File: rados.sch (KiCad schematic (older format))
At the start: 1 part

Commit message: More schematics, some layout
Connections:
- net CS0: now reaches SHIELD1.10 (D10)
- net SD_CD: now reaches SHIELD1.14 (D14-TX3)
- net Z-EN: now reaches SHIELD1.15 (D15-RX3)
- net Y-DIR: now reaches SHIELD1.16 (D16-TX2)
- net Y-STEP: now reaches SHIELD1.17 (D17-RX2)
- net Z-STEP: now reaches SHIELD1.2 (D2)
- net SDA: now reaches SHIELD1.20 (D20-SDA)
- net SCL: now reaches SHIELD1.21 (D21-SCL)
- net Y-EN: now reaches SHIELD1.22 (D22)
- net X-DIR: now reaches SHIELD1.23 (D23)
- net X-STEP: now reaches SHIELD1.24 (D24)
- net X-EN: now reaches SHIELD1.26 (D26)
- net X-: now reaches SHIELD1.28 (D28)
- net Z-DIR: now reaches SHIELD1.3 (D3)
- net Y-: now reaches SHIELD1.30 (D30)
- net Z-: now reaches SHIELD1.32 (D32)
- net X+: now reaches SHIELD1.34 (D34)
- net Y+: now reaches SHIELD1.36 (D36)
- net Z+: now reaches SHIELD1.38 (D38)
- net CS1: now reaches SHIELD1.4 (D4)
- net LCD_RS: now reaches SHIELD1.42 (D42)
- net LCD_E: now reaches SHIELD1.43 (D43)
- net LCD_4: now reaches SHIELD1.44 (D44)
- net LCD_5: now reaches SHIELD1.45 (D45)
- net LCD_6: now reaches SHIELD1.46 (D46)
- net LCD_7: now reaches SHIELD1.47 (D47)
- net ENC_SW: now reaches SHIELD1.48 (D48)
- net E3-EN: now reaches SHIELD1.49 (D49)
- net ENC_B: now reaches SHIELD1.50 (D50-MISO)
- net E3-STEP: now reaches SHIELD1.51 (D51-MOSI)
- net ENC_A: now reaches SHIELD1.52 (D52-SCK)
- net E3-DIR: now reaches SHIELD1.53 (D53-SS)
- net T0: now reaches SHIELD1.AD0
- net T1: now reaches SHIELD1.AD1
- net E2-STEP: now reaches SHIELD1.AD10
- net E2-EN: now reaches SHIELD1.AD11
- net T2: now reaches SHIELD1.AD2
- net T3: now reaches SHIELD1.AD3
- net T4: now reaches SHIELD1.AD4
- net E1-DIR: now reaches SHIELD1.AD6
- net E1-STEP: now reaches SHIELD1.AD7
- net E1-EN: now reaches SHIELD1.AD8
- net E2-DIR: now reaches SHIELD1.AD9
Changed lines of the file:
@@
 	1    0    0    -1
 $EndComp
-Text GLabel 3100 2200 0    47   Input ~ 0
+Text GLabel 3000 2200 0    47   Input ~ 0
 RESET
 $Comp
@@
 L +3.3V #PWR02
 U 1 1 568A9448
-P 2700 2275
-F 0 "#PWR02" H 2700 2125 50  0001 C CNN
-F 1 "+3.3V" H 2718 2449 50  0000 C CNN
-F 2 "" H 2700 2275 50  0000 C CNN
-F 3 "" H 2700 2275 50  0000 C CNN
-	1    2700 2275
-	1    0    0    -1
-$EndComp
-Wire Wire Line
-	2700 2300 3100 2300
-Wire Wire Line
-	2700 2300 2700 2275
+P 2650 2275
+F 0 "#PWR02" H 2650 2125 50  0001 C CNN
+F 1 "+3.3V" H 2625 2400 50  0000 C CNN
+F 2 "" H 2650 2275 50  0000 C CNN
+F 3 "" H 2650 2275 50  0000 C CNN
+	1    2650 2275
+	1    0    0    -1
+$EndComp
+Wire Wire Line
+	2650 2300 3100 2300
 $Comp
 L +5V #PWR03
@@
 P 2525 2400
 F 0 "#PWR03" H 2525 2250 50  0001 C CNN
-F 1 "+5V" H 2543 2574 50  0000 C CNN
+F 1 "+5V" H 2500 2525 50  0000 C CNN
 F 2 "" H 2525 2400 50  0000 C CNN
 F 3 "" H 2525 2400 50  0000 C CNN
@@
 F1 "power.sch" 59
 $EndSheet
-Text GLabel 3100 2700 0    47   Input ~ 0
+Text GLabel 3000 2700 0    47   Input ~ 0
 ARDUINO-VIN
 $Sheet
@@
 F1 "misc.sch" 60
 $EndSheet
+Text GLabel 5100 2300 2    47   Output ~ 0
+CS0
+Text GLabel 5100 3000 2    47   Output ~ 0
+CS1
+Wire Wire Line
+	5100 3000 5000 3000
+Wire Wire Line
+	5100 2300 5000 2300
+Text GLabel 5100 3100 2    47   Output ~ 0
+Z-DIR
+Text GLabel 5100 3200 2    47   Output ~ 0
+Z-STEP
+Wire Wire Line
+	5000 3100 5100 3100
+Wire Wire Line
+	5000 3200 5100 3200
+Text GLabel 5125 3600 2    47   Input ~ 0
+SD_CD
+Text GLabel 5125 3700 2    47   Output ~ 0
+Z-EN
+Text GLabel 5125 3800 2    47   Output ~ 0
+Y-DIR
+Text GLabel 5125 3900 2    47   Output ~ 0
+Y-STEP
+Text GLabel 5125 4200 2    47   BiDi ~ 0
+SDA
+Text GLabel 5125 4300 2    47   BiDi ~ 0
+SCL
+$Comp
+L +5V #PWR?
+U 1 1 568ECF51
+P 5000 4650
+F 0 "#PWR?" H 5000 4500 50  0001 C CNN
+F 1 "+5V" H 5018 4824 50  0000 C CNN
+F 2 "" H 5000 4650 50  0000 C CNN
+F 3 "" H 5000 4650 50  0000 C CNN
+	1    5000 4650
+	1    0    0    -1
+$EndComp
+Wire Wire Line
+	5125 3600 5000 3600
+Wire Wire Line
+	5125 3700 5000 3700
+Wire Wire Line
+	5125 3800 5000 3800
+Wire Wire Line
+	5125 3900 5000 3900
+Wire Wire Line
+	5000 4200 5125 4200
+Wire Wire Line
+	5125 4300 5000 4300
+Wire Wire Line
+	5000 4650 5000 4850
+Connection ~ 5000 4750
+Text GLabel 5125 5050 2    47   Output ~ 0
+Y-EN
+Text GLabel 5125 5150 2    47   Output ~ 0
+X-DIR
+Text GLabel 5125 5250 2    47   Output ~ 0
+X-STEP
+Text GLabel 5125 5450 2    47   Output ~ 0
+X-EN
+Text GLabel 5125 5650 2    47   Input ~ 0
+X-
+Text GLabel 5125 5900 2    47   Input ~ 0
+Y-
+Text GLabel 5125 6100 2    47   Input ~ 0
+Z-
+Text GLabel 5125 6300 2    47   Input ~ 0
+X+
+Text GLabel 5125 6500 2    47   Input ~ 0
+Y+
+Text GLabel 3000 6600 0    47   Input ~ 0
+Z+
+Wire Wire Line
+	5000 5050 5125 5050
+Wire Wire Line
+	5125 5150 5000 5150
+Wire Wire Line
+	5000 5250 5125 5250
+Wire Wire Line
+	5000 5450 5125 5450
+Wire Wire Line
+	5125 5650 5000 5650
+Wire Wire Line
+	5000 5900 5125 5900
+Wire Wire Line
+	5125 6100 5000 6100
+Wire Wire Line
+	5000 6300 5125 6300
+Wire Wire Line
+	5125 6500 5000 6500
+Wire Wire Line
+	3000 6600 3100 6600
+Text GLabel 3000 6150 0    47   BiDi ~ 0
+LCD_RS
+Text GLabel 3000 6050 0    47   BiDi ~ 0
+LCD_E
+Text GLabel 3000 5950 0    47   BiDi ~ 0
+LCD_4
+Text GLabel 3000 5850 0    47   BiDi ~ 0
+LCD_5
+Text GLabel 3000 5750 0    47   BiDi ~ 0
+LCD_6
+Text GLabel 3000 5650 0    47   BiDi ~ 0
+LCD_7
+Text GLabel 3000 5550 0    47   BiDi ~ 0
+ENC_SW
+Text GLabel 3000 5300 0    47   BiDi ~ 0
+ENC_B
+Text GLabel 3000 5100 0    47   BiDi ~ 0
+ENC_A
+Wire Wire Line
+	3000 6150 3100 6150
+Wire Wire Line
+	3100 6050 3000 6050
+Wire Wire Line
+	3000 5950 3100 5950
+Wire Wire Line
+	3100 5850 3000 5850
+Wire Wire Line
+	3000 5750 3100 5750
+Wire Wire Line
+	3100 5650 3000 5650
+Wire Wire Line
+	3000 5550 3100 5550
+Wire Wire Line
+	3000 5300 3100 5300
+Wire Wire Line
+	3100 5100 3000 5100
+Text GLabel 3000 5450 0    47   Output ~ 0
+E3-EN
+Text GLabel 3000 5200 0    47   Output ~ 0
+E3-STEP
+Text GLabel 3000 5000 0    47   Output ~ 0
+E3-DIR
+Wire Wire Line
+	3000 5000 3100 5000
+Wire Wire Line
+	3100 5200 3000 5200
+Wire Wire Line
+	3000 5450 3100 5450
+$Comp
+L GND #PWR?
+U 1 1 568EE3CA
+P 3100 4850
+F 0 "#PWR?" H 3100 4600 50  0001 C CNN
+F 1 "GND" H 3108 4676 50  0000 C CNN
+F 2 "" H 3100 4850 50  0000 C CNN
+F 3 "" H 3100 4850 50  0000 C CNN
+	1    3100 4850
+	1    0    0    -1
+$EndComp
+Wire Wire Line
+	3100 4850 3100 4750
+Connection ~ 3100 4850
+Text GLabel 3000 4000 0    47   Output ~ 0
+E2-STEP
+Text GLabel 3000 4100 0    47   Output ~ 0
+E2-EN
+Text GLabel 3000 3900 0    47   Output ~ 0
+E2-DIR
+Wire Wire Line
+	3000 4100 3100 4100
+Wire Wire Line
+	3100 4000 3000 4000
+Wire Wire Line
+	3000 3900 3100 3900
+Text GLabel 3000 3600 0    47   Output ~ 0
+E1-STEP
+Text GLabel 3000 3800 0    47   Output ~ 0
+E1-EN
+Text GLabel 3000 3500 0    47   Output ~ 0
+E1-DIR
+Wire Wire Line
+	3000 3800 3100 3800
+Wire Wire Line
+	3100 3600 3000 3600
+Wire Wire Line
+	3000 3500 3100 3500
+Wire Wire Line
+	3000 2700 3100 2700
+Wire Wire Line
+	2650 2300 2650 2275
+Wire Wire Line
+	3000 2200 3100 2200
+Text GLabel 3000 2900 0    47   Input ~ 0
+T0
+Text GLabel 3000 3000 0    47   Input ~ 0
+T1
+Text GLabel 3000 3100 0    47   Input ~ 0
+T2
+Text GLabel 3000 3200 0    47   Input ~ 0
+T3
+Text GLabel 3000 3300 0    47   Input ~ 0
+T4
+Wire Wire Line
+	3000 2900 3100 2900
+Wire Wire Line
+	3100 3000 3000 3000
+Wire Wire Line
+	3000 3100 3100 3100
+Wire Wire Line
+	3100 3200 3000 3200
+Wire Wire Line
+	3000 3300 3100 3300
 $EndSCHEMATC

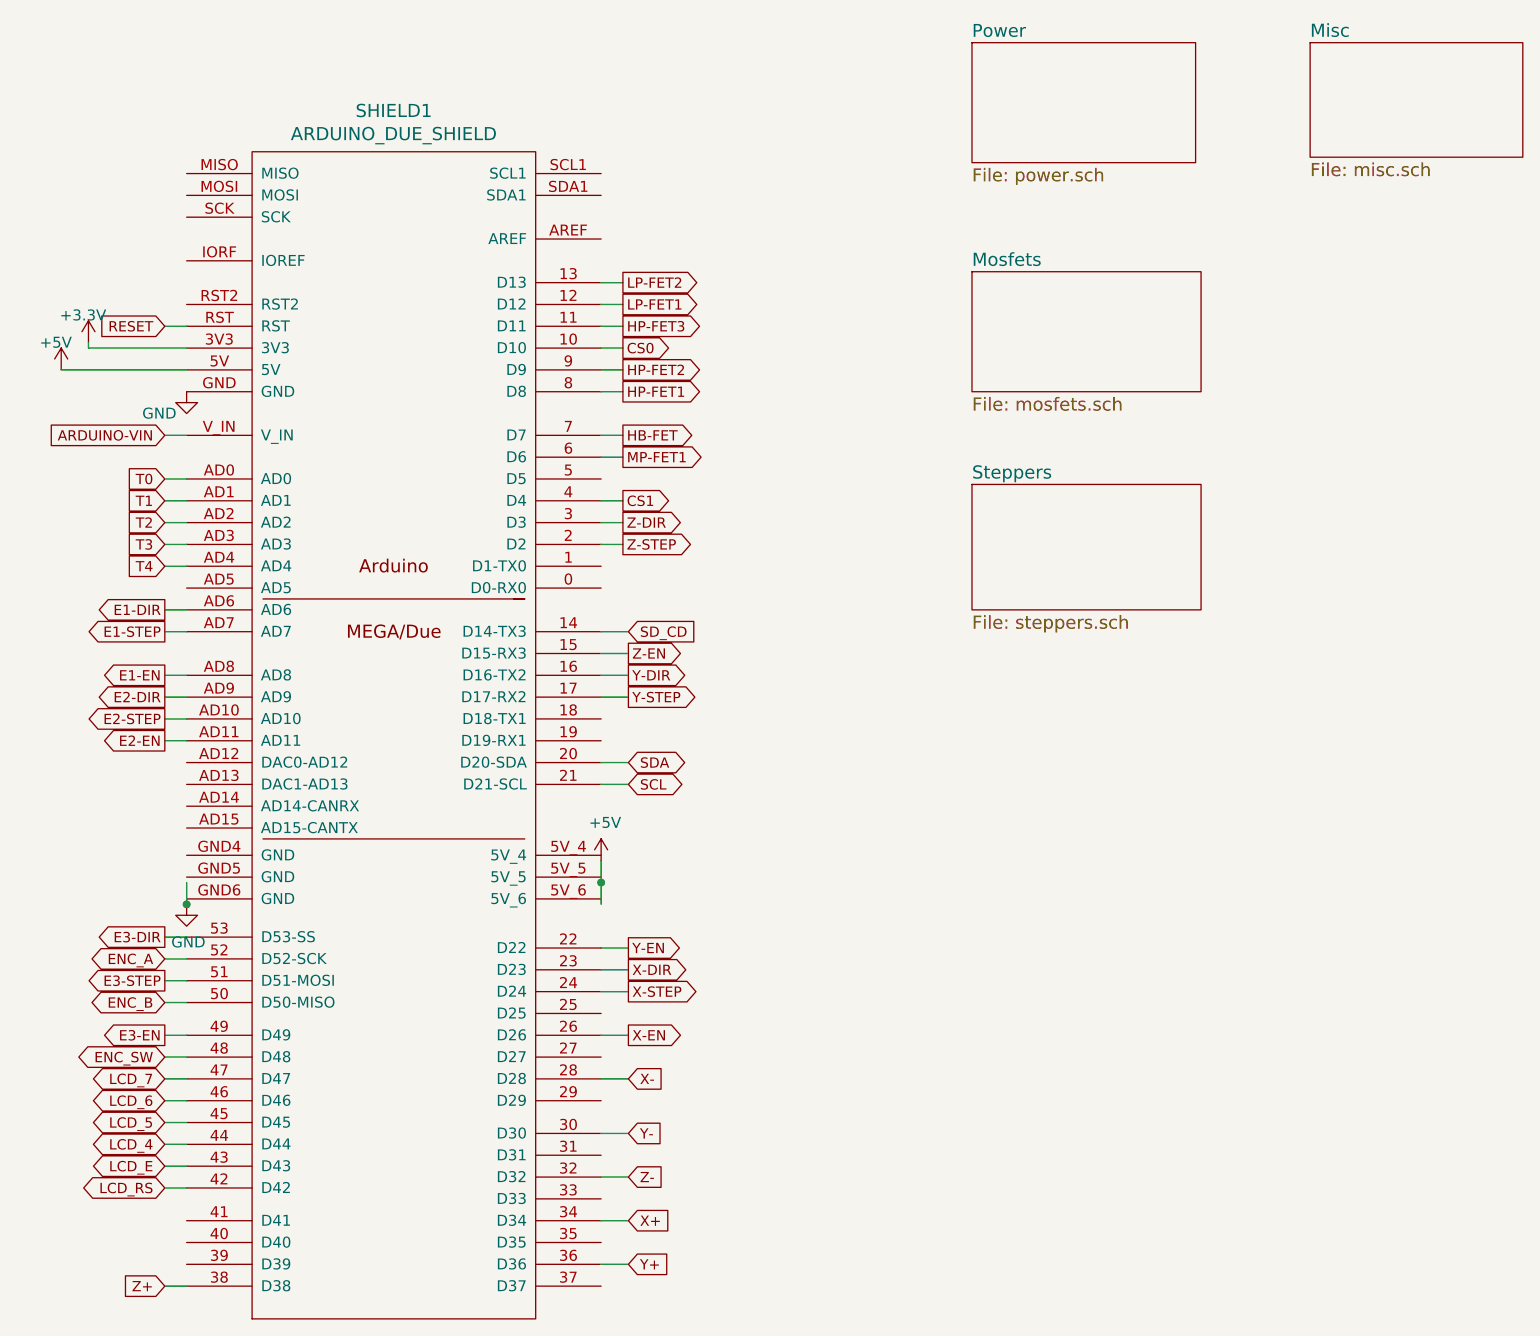
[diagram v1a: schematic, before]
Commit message: more placement and routing
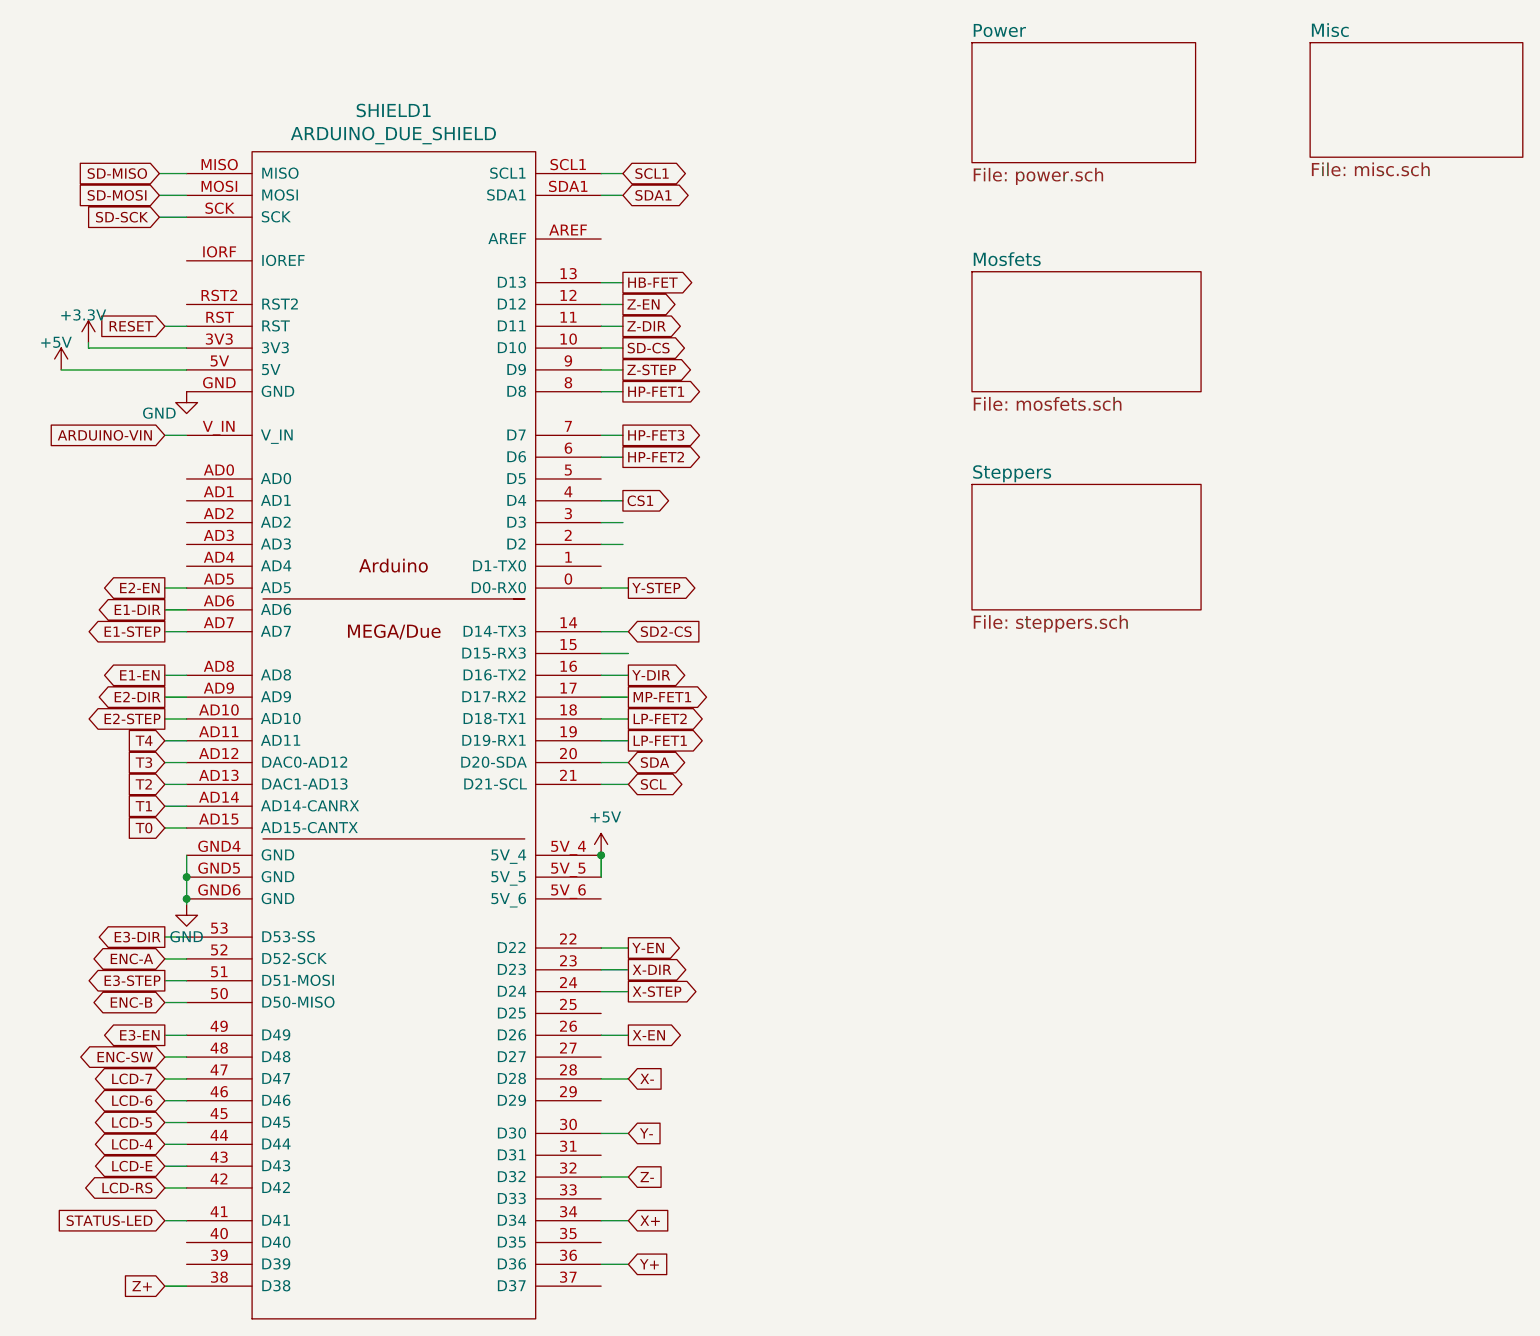
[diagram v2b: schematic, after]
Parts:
- SHIELD1: footprint arduino-footprint:ARDUINO_MEGA_DUE_SHIELD_FOOTPRINT_RMC -> arduino-footprint:ARDUINO_MEGA_DUE_SHIELD_FOOTPRINT_OTH2
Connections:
- net labels added: ENC-A, ENC-B, ENC-SW, LCD-4, LCD-5, LCD-6, LCD-7, LCD-E, LCD-RS, SCL1, SD-CS, SD-MISO, SD-MOSI, SD-SCK, SD2-CS, SDA1, STATUS-LED
- net labels removed: CS0, ENC_A, ENC_B, ENC_SW, LCD_4, LCD_5, LCD_6, LCD_7, LCD_E, LCD_RS, SD_CD
- wire segments 57 -> 66
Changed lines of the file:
@@
 EESchema Schematic File Version 2
+LIBS:led_reverse
 LIBS:arduino_shieldsNCL
 LIBS:otheruse_transistors
@@
 F 0 "SHIELD1" H 4050 7087 60  0000 C CNN
 F 1 "ARDUINO_DUE_SHIELD" H 4050 6981 60  0000 C CNN
-F 2 "arduino-footprint:ARDUINO_MEGA_DUE_SHIELD_FOOTPRINT_RMC" H 4100 4150 60  0001 C CNN
+F 2 "arduino-footprint:ARDUINO_MEGA_DUE_SHIELD_FOOTPRINT_OTH2" H 4100 4150 60  0001 C CNN
 F 3 "" H 4100 4150 60  0000 C CNN
 	1    4100 4150
@@
 F1 "mosfets.sch" 60
 $EndSheet
-Text GLabel 5100 2700 2    47   Output ~ 0
+Text GLabel 5100 2000 2    47   Output ~ 0
 HB-FET
 Text GLabel 5100 2500 2    47   Output ~ 0
 HP-FET1
-Text GLabel 5100 2400 2    47   Output ~ 0
+Text GLabel 5100 2800 2    47   Output ~ 0
 HP-FET2
-Text GLabel 5100 2200 2    47   Output ~ 0
+Text GLabel 5100 2700 2    47   Output ~ 0
 HP-FET3
-Text GLabel 5100 2800 2    47   Output ~ 0
+Text GLabel 5125 3900 2    47   Output ~ 0
 MP-FET1
-Text GLabel 5100 2100 2    47   Output ~ 0
+Text GLabel 5125 4100 2    47   Output ~ 0
 LP-FET1
-Text GLabel 5100 2000 2    47   Output ~ 0
+Text GLabel 5125 4000 2    47   Output ~ 0
 LP-FET2
 Wire Wire Line
@@
 $EndSheet
 Text GLabel 5100 2300 2    47   Output ~ 0
-CS0
+SD-CS
 Text GLabel 5100 3000 2    47   Output ~ 0
 CS1
@@
 Wire Wire Line
 	5100 2300 5000 2300
-Text GLabel 5100 3100 2    47   Output ~ 0
+Text GLabel 5100 2200 2    47   Output ~ 0
 Z-DIR
-Text GLabel 5100 3200 2    47   Output ~ 0
+Text GLabel 5100 2400 2    47   Output ~ 0
 Z-STEP
 Wire Wire Line
@@
 	5000 3200 5100 3200
 Text GLabel 5125 3600 2    47   Input ~ 0
-SD_CD
-Text GLabel 5125 3700 2    47   Output ~ 0
+SD2-CS
+Text GLabel 5100 2100 2    47   Output ~ 0
 Z-EN
 Text GLabel 5125 3800 2    47   Output ~ 0
 Y-DIR
-Text GLabel 5125 3900 2    47   Output ~ 0
+Text GLabel 5125 3400 2    47   Output ~ 0
 Y-STEP
 Text GLabel 5125 4200 2    47   BiDi ~ 0
@@
 SCL
 $Comp
-L +5V #PWR?
+L +5V #PWR04
 U 1 1 568ECF51
-P 5000 4650
-F 0 "#PWR?" H 5000 4500 50  0001 C CNN
-F 1 "+5V" H 5018 4824 50  0000 C CNN
-F 2 "" H 5000 4650 50  0000 C CNN
-F 3 "" H 5000 4650 50  0000 C CNN
-	1    5000 4650
+P 5000 4625
+F 0 "#PWR04" H 5000 4475 50  0001 C CNN
+F 1 "+5V" H 5018 4799 50  0000 C CNN
+F 2 "" H 5000 4625 50  0000 C CNN
+F 3 "" H 5000 4625 50  0000 C CNN
+	1    5000 4625
 	1    0    0    -1
 $EndComp
@@
 	5125 4300 5000 4300
 Wire Wire Line
-	5000 4650 5000 4850
-Connection ~ 5000 4750
+	5000 4625 5000 4725
 Text GLabel 5125 5050 2    47   Output ~ 0
 Y-EN
@@
 	3000 6600 3100 6600
 Text GLabel 3000 6150 0    47   BiDi ~ 0
-LCD_RS
+LCD-RS
 Text GLabel 3000 6050 0    47   BiDi ~ 0
-LCD_E
+LCD-E
 Text GLabel 3000 5950 0    47   BiDi ~ 0
-LCD_4
+LCD-4
 Text GLabel 3000 5850 0    47   BiDi ~ 0
-LCD_5
+LCD-5
 Text GLabel 3000 5750 0    47   BiDi ~ 0
-LCD_6
+LCD-6
 Text GLabel 3000 5650 0    47   BiDi ~ 0
-LCD_7
+LCD-7
 Text GLabel 3000 5550 0    47   BiDi ~ 0
-ENC_SW
+ENC-SW
 Text GLabel 3000 5300 0    47   BiDi ~ 0
-ENC_B
+ENC-B
 Text GLabel 3000 5100 0    47   BiDi ~ 0
-ENC_A
+ENC-A
 Wire Wire Line
 	3000 6150 3100 6150
@@
 	3000 5450 3100 5450
 $Comp
-L GND #PWR?
+L GND #PWR05
 U 1 1 568EE3CA
 P 3100 4850
-F 0 "#PWR?" H 3100 4600 50  0001 C CNN
-F 1 "GND" H 3108 4676 50  0000 C CNN
+F 0 "#PWR05" H 3100 4600 50  0001 C CNN
+F 1 "GND" H 3100 4700 50  0000 C CNN
 F 2 "" H 3100 4850 50  0000 C CNN
 F 3 "" H 3100 4850 50  0000 C CNN
@@
 $EndComp
 Wire Wire Line
-	3100 4850 3100 4750
-Connection ~ 3100 4850
+	3100 4625 3100 4850
 Text GLabel 3000 4000 0    47   Output ~ 0
 E2-STEP
-Text GLabel 3000 4100 0    47   Output ~ 0
+Text GLabel 3000 3400 0    47   Output ~ 0
 E2-EN
 Text GLabel 3000 3900 0    47   Output ~ 0
 E2-DIR
 Wire Wire Line
-	3000 4100 3100 4100
+	3000 3400 3100 3400
 Wire Wire Line
 	3100 4000 3000 4000
@@
 Wire Wire Line
 	3000 2200 3100 2200
-Text GLabel 3000 2900 0    47   Input ~ 0
+Text GLabel 3000 4500 0    47   Input ~ 0
 T0
-Text GLabel 3000 3000 0    47   Input ~ 0
+Text GLabel 3000 4400 0    47   Input ~ 0
 T1
-Text GLabel 3000 3100 0    47   Input ~ 0
+Text GLabel 3000 4300 0    47   Input ~ 0
 T2
-Text GLabel 3000 3200 0    47   Input ~ 0
+Text GLabel 3000 4200 0    47   Input ~ 0
 T3
-Text GLabel 3000 3300 0    47   Input ~ 0
+Text GLabel 3000 4100 0    47   Input ~ 0
 T4
 Wire Wire Line
-	3000 2900 3100 2900
-Wire Wire Line
-	3100 3000 3000 3000
-Wire Wire Line
-	3000 3100 3100 3100
-Wire Wire Line
-	3100 3200 3000 3200
-Wire Wire Line
-	3000 3300 3100 3300
+	3000 4500 3100 4500
+Wire Wire Line
+	3100 4400 3000 4400
+Wire Wire Line
+	3000 4300 3100 4300
+Wire Wire Line
+	3100 4200 3000 4200
+Wire Wire Line
+	3000 4100 3100 4100
+Text GLabel 3000 6300 0    47   Input ~ 0
+STATUS-LED
+Wire Wire Line
+	3000 6300 3100 6300
+Text GLabel 5100 1500 2    47   BiDi ~ 0
+SCL1
+Text GLabel 5100 1600 2    47   BiDi ~ 0
+SDA1
+Wire Wire Line
+	5100 1500 5000 1500
+Wire Wire Line
+	5000 1600 5100 1600
+Text GLabel 2975 1500 0    47   Input ~ 0
+SD-MISO
+Text GLabel 2975 1600 0    47   Input ~ 0
+SD-MOSI
+Text GLabel 2975 1700 0    47   Input ~ 0
+SD-SCK
+Wire Wire Line
+	2975 1500 3100 1500
+Wire Wire Line
+	3100 1600 2975 1600
+Wire Wire Line
+	2975 1700 3100 1700
+Connection ~ 3100 4725
+Connection ~ 3100 4825
+Connection ~ 5000 4625
+Wire Wire Line
+	5125 4100 5000 4100
+Wire Wire Line
+	5000 4000 5125 4000
+Wire Wire Line
+	5125 3400 5000 3400
 $EndSCHEMATC
